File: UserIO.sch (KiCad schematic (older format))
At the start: 17 parts, among them SW1 PF0, SW2 PF1, SW3 PF2, SW4 PF3, SW5 RST, U1 ATXMEGA128A1U-AU

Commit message: Reannotate
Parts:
- renumbered C14 to C4, C15 to C5, C16 to C6, C17 to C7, DS1 to DS2, DS2 to DS3, DS3 to DS4, DS4 to DS5, R19 to R15, R10 to R16, R11 to R17, SW5 to SW1, SW1 to SW2, SW2 to SW3, SW3 to SW4, SW4 to SW5
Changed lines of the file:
@@
 $EndComp
 $Comp
-L TACT-TE-FSMSM SW1
+L TACT-TE-FSMSM SW2
 U 1 1 56EFE88A
 P 7250 4900
-F 0 "SW1" H 7400 5000 50  0000 C CNN
+F 0 "SW2" H 7400 5000 50  0000 C CNN
 F 1 "PF0" H 7100 5000 50  0000 C CNN
 F 2 "manuf:TE-FSMSM" H 7250 4700 60  0001 C CNN
@@
 P 4400 5950
 AR Path="/56EFE892" Ref="C?"  Part="1"
-AR Path="/56EFC605/56EFE892" Ref="C14"  Part="1"
-F 0 "C14" H 4450 6050 50  0000 L CNN
+AR Path="/56EFC605/56EFE892" Ref="C4"  Part="1"
+F 0 "C4" H 4450 6050 50  0000 L CNN
 F 1 "100n" H 4450 5850 50  0000 L CNN
 F 2 "IPC7351-Nominal:CAPC1005X55" H 4400 5950 50  0001 C CNN
@@
 PF0/~DFUEN
 $Comp
-L TACT-TE-FSMSM SW2
+L TACT-TE-FSMSM SW3
 U 1 1 56EFE8A1
 P 7250 5100
-F 0 "SW2" H 7400 5200 50  0000 C CNN
+F 0 "SW3" H 7400 5200 50  0000 C CNN
 F 1 "PF1" H 7100 5200 50  0000 C CNN
 F 2 "manuf:TE-FSMSM" H 7250 4900 60  0001 C CNN
@@
 $EndComp
 $Comp
-L TACT-TE-FSMSM SW3
+L TACT-TE-FSMSM SW4
 U 1 1 56EFE8A9
 P 7250 5300
-F 0 "SW3" H 7400 5400 50  0000 C CNN
+F 0 "SW4" H 7400 5400 50  0000 C CNN
 F 1 "PF2" H 7100 5400 50  0000 C CNN
 F 2 "manuf:TE-FSMSM" H 7250 5100 60  0001 C CNN
@@
 $EndComp
 $Comp
-L TACT-TE-FSMSM SW4
+L TACT-TE-FSMSM SW5
 U 1 1 56EFE8B1
 P 7250 5500
-F 0 "SW4" H 7400 5600 50  0000 C CNN
+F 0 "SW5" H 7400 5600 50  0000 C CNN
 F 1 "PF3" H 7100 5600 50  0000 C CNN
 F 2 "manuf:TE-FSMSM" H 7250 5300 60  0001 C CNN
@@
 P 4700 5950
 AR Path="/56EFE8B9" Ref="C?"  Part="1"
-AR Path="/56EFC605/56EFE8B9" Ref="C15"  Part="1"
-F 0 "C15" H 4750 6050 50  0000 L CNN
+AR Path="/56EFC605/56EFE8B9" Ref="C5"  Part="1"
+F 0 "C5" H 4750 6050 50  0000 L CNN
 F 1 "100n" H 4750 5850 50  0000 L CNN
 F 2 "IPC7351-Nominal:CAPC1005X55" H 4700 5950 50  0001 C CNN
@@
 P 5000 5950
 AR Path="/56EFE8C1" Ref="C?"  Part="1"
-AR Path="/56EFC605/56EFE8C1" Ref="C16"  Part="1"
-F 0 "C16" H 5050 6050 50  0000 L CNN
+AR Path="/56EFC605/56EFE8C1" Ref="C6"  Part="1"
+F 0 "C6" H 5050 6050 50  0000 L CNN
 F 1 "100n" H 5050 5850 50  0000 L CNN
 F 2 "IPC7351-Nominal:CAPC1005X55" H 5000 5950 50  0001 C CNN
@@
 P 5300 5950
 AR Path="/56EFE8C9" Ref="C?"  Part="1"
-AR Path="/56EFC605/56EFE8C9" Ref="C17"  Part="1"
-F 0 "C17" H 5350 6050 50  0000 L CNN
+AR Path="/56EFC605/56EFE8C9" Ref="C7"  Part="1"
+F 0 "C7" H 5350 6050 50  0000 L CNN
 F 1 "100n" H 5350 5850 50  0000 L CNN
 F 2 "IPC7351-Nominal:CAPC1005X55" H 5300 5950 50  0001 C CNN
@@
 PF3
 $Comp
-L TACT-TE-FSMSM SW5
+L TACT-TE-FSMSM SW1
 U 1 1 56EFE8EC
 P 7250 4500
-F 0 "SW5" H 7250 4720 50  0000 C CNN
+F 0 "SW1" H 7250 4720 50  0000 C CNN
 F 1 "RST" H 7250 4629 50  0000 C CNN
 F 2 "manuf:TE-FSMSM" H 7250 4300 60  0001 C CNN
@@
 $EndComp
 $Comp
-L LED-0603 DS1
+L LED-0603 DS2
 U 1 1 56EFE8F4
 P 5450 4000
-F 0 "DS1" H 5600 4046 50  0000 L CNN
+F 0 "DS2" H 5600 4046 50  0000 L CNN
 F 1 "PF4" H 5600 3955 50  0000 L CNN
 F 2 "smd-semi:LED-0603" H 5450 3850 50  0001 C CNN
@@
 $EndComp
 $Comp
-L LED-0603 DS2
+L LED-0603 DS3
 U 1 1 56EFE902
 P 5850 4000
-F 0 "DS2" H 6000 4046 50  0000 L CNN
+F 0 "DS3" H 6000 4046 50  0000 L CNN
 F 1 "PF5" H 6000 3955 50  0000 L CNN
 F 2 "smd-semi:LED-0603" H 5850 3850 50  0001 C CNN
@@
 $EndComp
 $Comp
-L LED-0603 DS3
+L LED-0603 DS4
 U 1 1 56EFE910
 P 6250 4000
-F 0 "DS3" H 6400 4046 50  0000 L CNN
+F 0 "DS4" H 6400 4046 50  0000 L CNN
 F 1 "PF6" H 6400 3955 50  0000 L CNN
 F 2 "smd-semi:LED-0603" H 6250 3850 50  0001 C CNN
@@
 $EndComp
 $Comp
-L LED-0603 DS4
+L LED-0603 DS5
 U 1 1 56EFE91E
 P 6650 4000
-F 0 "DS4" H 6800 4046 50  0000 L CNN
+F 0 "DS5" H 6800 4046 50  0000 L CNN
 F 1 "PF7" H 6800 3955 50  0000 L CNN
 F 2 "smd-semi:LED-0603" H 6650 3850 50  0001 C CNN
@@
 P 5450 3700
 AR Path="/56EFE930" Ref="R?"  Part="1"
-AR Path="/56EFC605/56EFE930" Ref="R19"  Part="1"
-F 0 "R19" H 5387 3654 50  0000 R CNN
+AR Path="/56EFC605/56EFE930" Ref="R15"  Part="1"
+F 0 "R15" H 5387 3654 50  0000 R CNN
 F 1 "3k3" H 5387 3745 50  0000 R CNN
 F 2 "IPC7351-Nominal:RESCAXE80P160X320X70-8" H 5450 3700 50  0001 C CNN
@@
 P 5850 3700
 AR Path="/56EFE938" Ref="R?"  Part="2"
-AR Path="/56EFC605/56EFE938" Ref="R19"  Part="2"
-F 0 "R19" H 5787 3654 50  0000 R CNN
+AR Path="/56EFC605/56EFE938" Ref="R15"  Part="2"
+F 0 "R15" H 5787 3654 50  0000 R CNN
 F 1 "3k3" H 5787 3745 50  0000 R CNN
 F 2 "IPC7351-Nominal:RESCAXE80P160X320X70-8" H 5850 3700 50  0001 C CNN
@@
 P 6250 3700
 AR Path="/56EFE940" Ref="R?"  Part="3"
-AR Path="/56EFC605/56EFE940" Ref="R19"  Part="3"
-F 0 "R19" H 6187 3654 50  0000 R CNN
+AR Path="/56EFC605/56EFE940" Ref="R15"  Part="3"
+F 0 "R15" H 6187 3654 50  0000 R CNN
 F 1 "3k3" H 6187 3745 50  0000 R CNN
 F 2 "IPC7351-Nominal:RESCAXE80P160X320X70-8" H 6250 3700 50  0001 C CNN
@@
 P 6650 3700
 AR Path="/56EFE948" Ref="R?"  Part="4"
-AR Path="/56EFC605/56EFE948" Ref="R19"  Part="4"
-F 0 "R19" H 6587 3654 50  0000 R CNN
+AR Path="/56EFC605/56EFE948" Ref="R15"  Part="4"
+F 0 "R15" H 6587 3654 50  0000 R CNN
 F 1 "3k3" H 6587 3745 50  0000 R CNN
 F 2 "IPC7351-Nominal:RESCAXE80P160X320X70-8" H 6650 3700 50  0001 C CNN
@@
 P 5650 4900
 AR Path="/56EFE950" Ref="R?"  Part="1"
-AR Path="/56EFC605/56EFE950" Ref="R10"  Part="1"
-F 0 "R10" V 5700 4700 50  0000 C CNN
+AR Path="/56EFC605/56EFE950" Ref="R16"  Part="1"
+F 0 "R16" V 5700 4700 50  0000 C CNN
 F 1 "100k" V 5700 5100 50  0000 C CNN
 F 2 "IPC7351-Nominal:RESCAXE80P160X320X70-8" H 5650 4900 50  0001 C CNN
@@
 P 6900 4700
 AR Path="/56EFE958" Ref="R?"  Part="2"
-AR Path="/56EFC605/56EFE958" Ref="R10"  Part="2"
-F 0 "R10" H 6837 4654 50  0000 R CNN
+AR Path="/56EFC605/56EFE958" Ref="R16"  Part="2"
+F 0 "R16" H 6837 4654 50  0000 R CNN
 F 1 "100k" H 6837 4745 50  0000 R CNN
 F 2 "IPC7351-Nominal:RESCAXE80P160X320X70-8" H 6900 4700 50  0001 C CNN
@@
 P 6600 4700
 AR Path="/56EFE960" Ref="R?"  Part="3"
-AR Path="/56EFC605/56EFE960" Ref="R10"  Part="3"
-F 0 "R10" H 6663 4654 50  0000 L CNN
+AR Path="/56EFC605/56EFE960" Ref="R16"  Part="3"
+F 0 "R16" H 6663 4654 50  0000 L CNN
 F 1 "100k" H 6663 4745 50  0000 L CNN
 F 2 "IPC7351-Nominal:RESCAXE80P160X320X70-8" H 6600 4700 50  0001 C CNN
@@
 P 5650 5100
 AR Path="/56EFE968" Ref="R?"  Part="4"
-AR Path="/56EFC605/56EFE968" Ref="R10"  Part="4"
-F 0 "R10" V 5700 4900 50  0000 C CNN
+AR Path="/56EFC605/56EFE968" Ref="R16"  Part="4"
+F 0 "R16" V 5700 4900 50  0000 C CNN
 F 1 "100k" V 5700 5300 50  0000 C CNN
 F 2 "IPC7351-Nominal:RESCAXE80P160X320X70-8" H 5650 5100 50  0001 C CNN
@@
 P 5650 5300
 AR Path="/56EFE970" Ref="R?"  Part="1"
-AR Path="/56EFC605/56EFE970" Ref="R11"  Part="1"
-F 0 "R11" V 5700 5100 50  0000 C CNN
+AR Path="/56EFC605/56EFE970" Ref="R17"  Part="1"
+F 0 "R17" V 5700 5100 50  0000 C CNN
 F 1 "100k" V 5700 5500 50  0000 C CNN
 F 2 "IPC7351-Nominal:RESCAXE80P160X320X70-8" H 5650 5300 50  0001 C CNN
@@
 P 5650 5500
 AR Path="/56EFE978" Ref="R?"  Part="4"
-AR Path="/56EFC605/56EFE978" Ref="R11"  Part="4"
-F 0 "R11" V 5700 5300 50  0000 C CNN
+AR Path="/56EFC605/56EFE978" Ref="R17"  Part="4"
+F 0 "R17" V 5700 5300 50  0000 C CNN
 F 1 "100k" V 5700 5700 50  0000 C CNN
 F 2 "IPC7351-Nominal:RESCAXE80P160X320X70-8" H 5650 5500 50  0001 C CNN
@@
 P 6300 4700
 AR Path="/56EFE980" Ref="R?"  Part="2"
-AR Path="/56EFC605/56EFE980" Ref="R11"  Part="2"
-F 0 "R11" H 6237 4654 50  0000 R CNN
+AR Path="/56EFC605/56EFE980" Ref="R17"  Part="2"
+F 0 "R17" H 6237 4654 50  0000 R CNN
 F 1 "100k" H 6237 4745 50  0000 R CNN
 F 2 "IPC7351-Nominal:RESCAXE80P160X320X70-8" H 6300 4700 50  0001 C CNN
@@
 P 6000 4700
 AR Path="/56EFE988" Ref="R?"  Part="3"
-AR Path="/56EFC605/56EFE988" Ref="R11"  Part="3"
-F 0 "R11" H 6063 4654 50  0000 L CNN
+AR Path="/56EFC605/56EFE988" Ref="R17"  Part="3"
+F 0 "R17" H 6063 4654 50  0000 L CNN
 F 1 "100k" H 6063 4745 50  0000 L CNN
 F 2 "IPC7351-Nominal:RESCAXE80P160X320X70-8" H 6000 4700 50  0001 C CNN

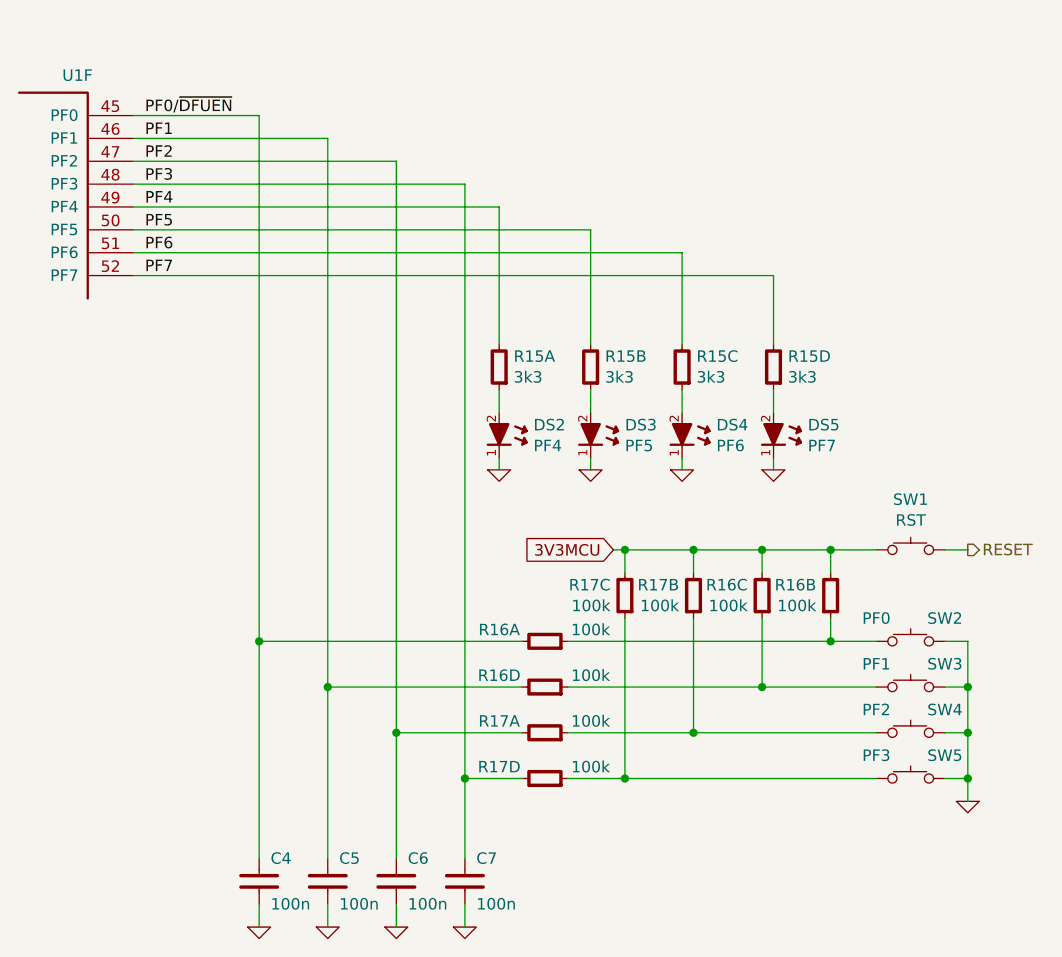
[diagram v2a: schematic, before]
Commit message: Schematic tidy-ups and add VBUS sense
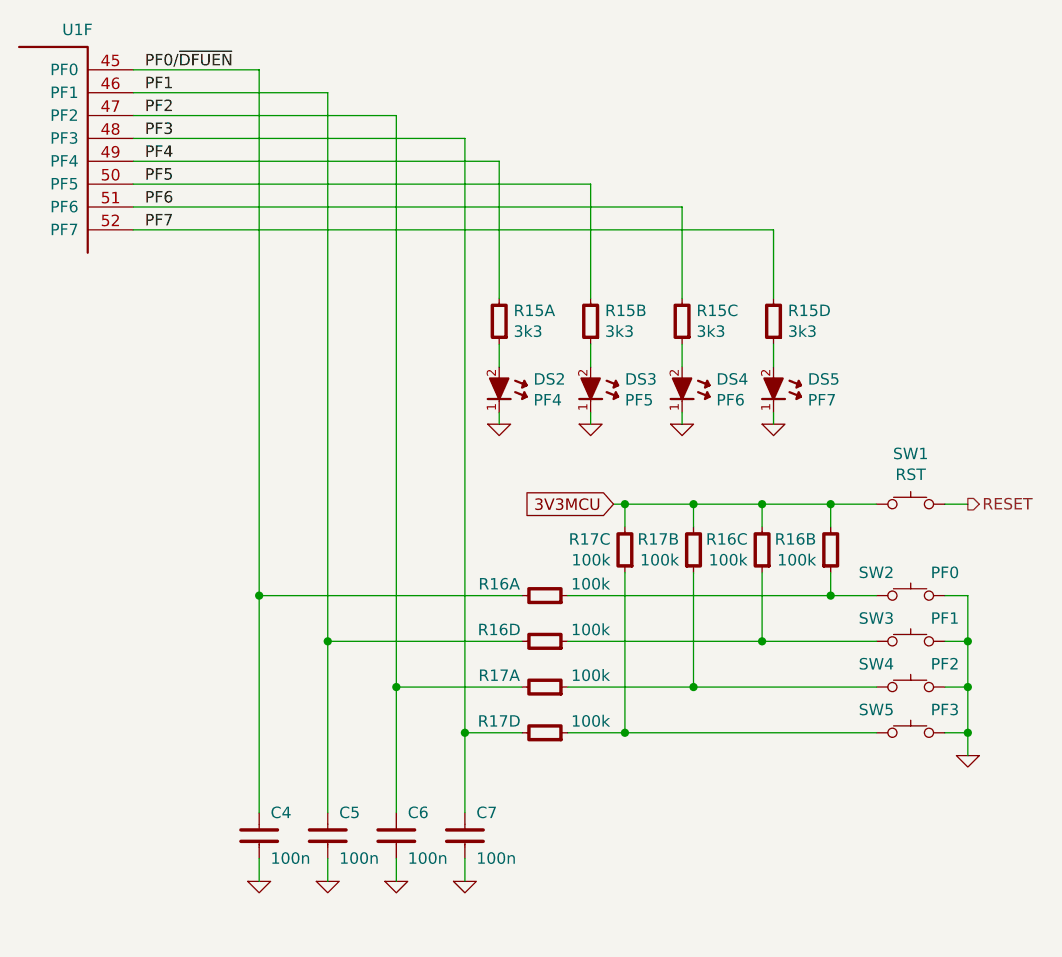
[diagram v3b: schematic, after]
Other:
- moved on the sheet: C4, C5, C6, C7, DS2, DS3, DS4, DS5, R15A, R15B, R15C, R15D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

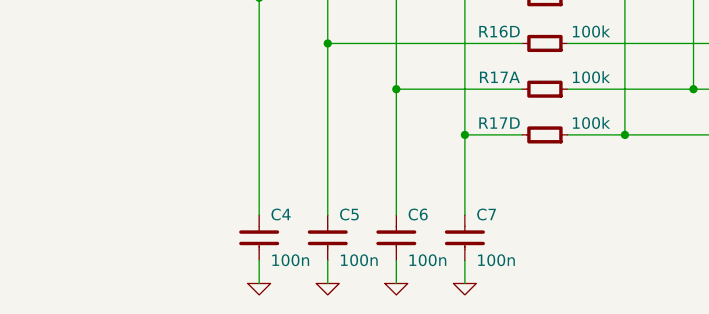
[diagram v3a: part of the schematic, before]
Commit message: Bugfix: debounce causes bootloader entry on power
Debounce capacitors were connected to ground, which held the IOs low at boot
for about 20ms. Capacitors are now connected to 3.3V instead.
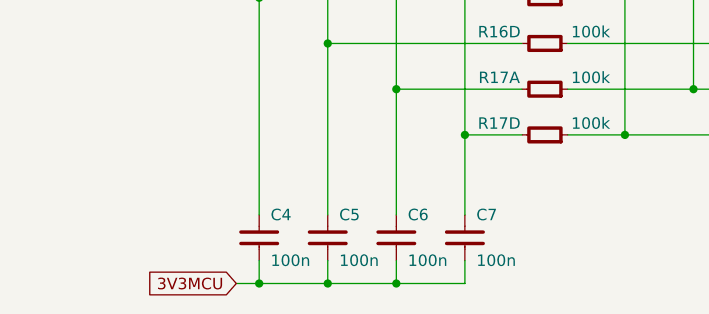
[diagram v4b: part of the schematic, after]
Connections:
- net 3V3MCU: now also C4.2, C5.2, C6.2, C7.2
- net GND: no longer C4.2, C5.2, C6.2, C7.2
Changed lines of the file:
@@
 LIBS:Vishay
 LIBS:Xilinx
+LIBS:semi-diode-Semtech
 LIBS:xmega-cache
 EELAYER 25 0
@@
 	1    0    0    -1
 $EndComp
-$Comp
-L GND #PWR?
-U 1 1 56EFE899
-P 4400 5950
-AR Path="/56EFE899" Ref="#PWR?"  Part="1"
-AR Path="/56EFC605/56EFE899" Ref="#PWR24"  Part="1"
-F 0 "#PWR24" H 4400 5950 30  0001 C CNN
-F 1 "GND" H 4400 5880 30  0001 C CNN
-F 2 "" H 4400 5950 60  0000 C CNN
-F 3 "" H 4400 5950 60  0000 C CNN
-	1    4400 5950
-	1    0    0    -1
-$EndComp
 Text Label 3900 2400 0    50   ~ 0
 PF0/~DFUEN
@@
 $Comp
 L GND #PWR?
-U 1 1 56EFE8D0
-P 4700 5950
-AR Path="/56EFE8D0" Ref="#PWR?"  Part="1"
-AR Path="/56EFC605/56EFE8D0" Ref="#PWR25"  Part="1"
-F 0 "#PWR25" H 4700 5950 30  0001 C CNN
-F 1 "GND" H 4700 5880 30  0001 C CNN
-F 2 "" H 4700 5950 60  0000 C CNN
-F 3 "" H 4700 5950 60  0000 C CNN
-	1    4700 5950
-	1    0    0    -1
-$EndComp
-$Comp
-L GND #PWR?
-U 1 1 56EFE8D6
-P 5000 5950
-AR Path="/56EFE8D6" Ref="#PWR?"  Part="1"
-AR Path="/56EFC605/56EFE8D6" Ref="#PWR26"  Part="1"
-F 0 "#PWR26" H 5000 5950 30  0001 C CNN
-F 1 "GND" H 5000 5880 30  0001 C CNN
-F 2 "" H 5000 5950 60  0000 C CNN
-F 3 "" H 5000 5950 60  0000 C CNN
-	1    5000 5950
-	1    0    0    -1
-$EndComp
-$Comp
-L GND #PWR?
-U 1 1 56EFE8DC
-P 5300 5950
-AR Path="/56EFE8DC" Ref="#PWR?"  Part="1"
-AR Path="/56EFC605/56EFE8DC" Ref="#PWR27"  Part="1"
-F 0 "#PWR27" H 5300 5950 30  0001 C CNN
-F 1 "GND" H 5300 5880 30  0001 C CNN
-F 2 "" H 5300 5950 60  0000 C CNN
-F 3 "" H 5300 5950 60  0000 C CNN
-	1    5300 5950
-	1    0    0    -1
-$EndComp
-$Comp
-L GND #PWR?
 U 1 1 56EFE8E2
 P 7500 5400
@@
 Text HLabel 7500 4300 2    50   Output ~ 0
 RESET
+Text GLabel 4300 5950 0    50   Input ~ 0
+3V3MCU
+Wire Wire Line
+	4300 5950 5300 5950
+Connection ~ 4400 5950
+Connection ~ 4700 5950
+Connection ~ 5000 5950
 $EndSCHEMATC

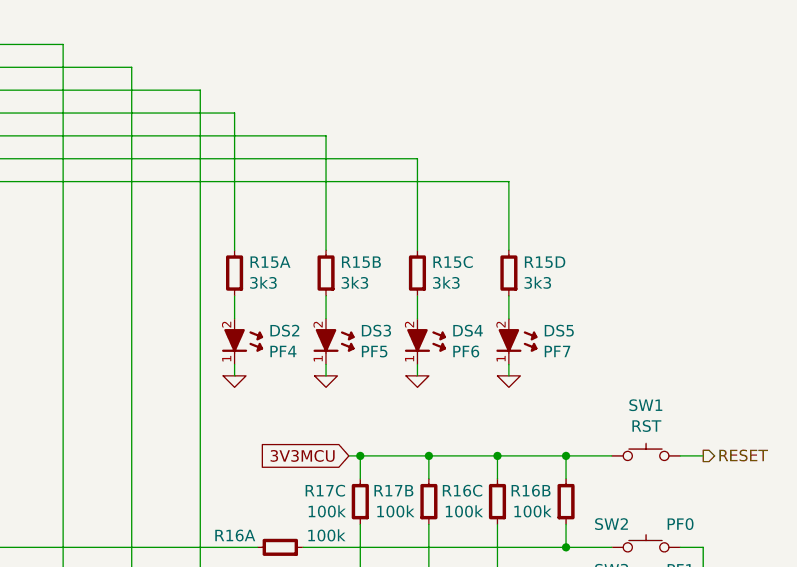
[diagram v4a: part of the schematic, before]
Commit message: Decrease LED current
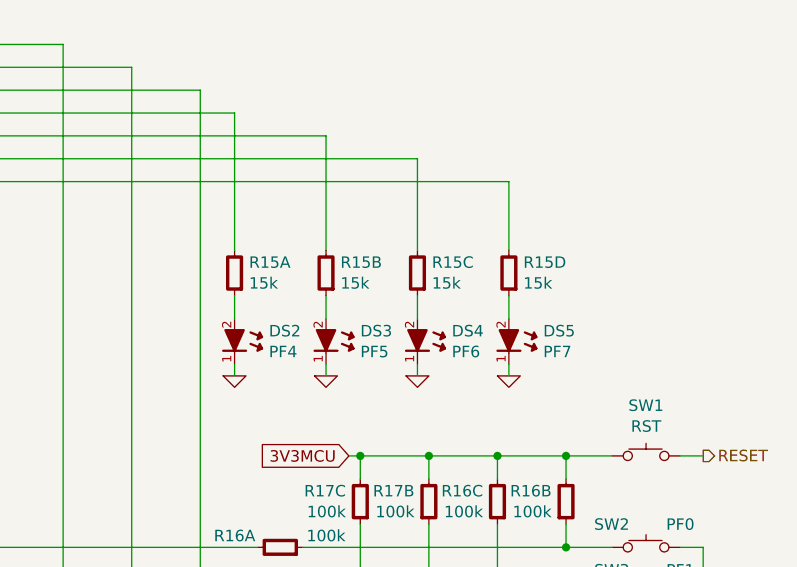
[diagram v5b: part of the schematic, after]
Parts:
- R15: value 3k3 -> 15k; BOM DIST DIGIKEY YC164J-3.3KCT-ND -> DIST DIGIKEY YC164J-15KCT-ND
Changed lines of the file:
@@
 AR Path="/56EFC605/56EFE930" Ref="R15"  Part="1"
 F 0 "R15" H 5387 3454 50  0000 R CNN
-F 1 "3k3" H 5387 3545 50  0000 R CNN
+F 1 "15k" H 5387 3545 50  0000 R CNN
 F 2 "IPC7351-Nominal:RESCAXE80P160X320X70-8" H 5450 3500 50  0001 C CNN
 F 3 "" H 5450 3550 60  0000 C CNN
-F 4 "DIST DIGIKEY YC164J-3.3KCT-ND" H 5450 3500 60  0001 C CNN "BOM"
+F 4 "DIST DIGIKEY YC164J-15KCT-ND" H 5450 3500 60  0001 C CNN "BOM"
 	1    5450 3500
 	-1   0    0    1
@@
 AR Path="/56EFC605/56EFE938" Ref="R15"  Part="2"
 F 0 "R15" H 5787 3454 50  0000 R CNN
-F 1 "3k3" H 5787 3545 50  0000 R CNN
+F 1 "15k" H 5787 3545 50  0000 R CNN
 F 2 "IPC7351-Nominal:RESCAXE80P160X320X70-8" H 5850 3500 50  0001 C CNN
 F 3 "" H 5850 3550 60  0000 C CNN
-F 4 "DIST DIGIKEY YC164J-3.3KCT-ND" H 5850 3500 60  0001 C CNN "BOM"
+F 4 "DIST DIGIKEY YC164J-15KCT-ND" H 5850 3500 60  0001 C CNN "BOM"
 	2    5850 3500
 	-1   0    0    1
@@
 AR Path="/56EFC605/56EFE940" Ref="R15"  Part="3"
 F 0 "R15" H 6187 3454 50  0000 R CNN
-F 1 "3k3" H 6187 3545 50  0000 R CNN
+F 1 "15k" H 6187 3545 50  0000 R CNN
 F 2 "IPC7351-Nominal:RESCAXE80P160X320X70-8" H 6250 3500 50  0001 C CNN
 F 3 "" H 6250 3550 60  0000 C CNN
-F 4 "DIST DIGIKEY YC164J-3.3KCT-ND" H 6250 3500 60  0001 C CNN "BOM"
+F 4 "DIST DIGIKEY YC164J-15KCT-ND" H 6250 3500 60  0001 C CNN "BOM"
 	3    6250 3500
 	-1   0    0    1
@@
 AR Path="/56EFC605/56EFE948" Ref="R15"  Part="4"
 F 0 "R15" H 6587 3454 50  0000 R CNN
-F 1 "3k3" H 6587 3545 50  0000 R CNN
+F 1 "15k" H 6587 3545 50  0000 R CNN
 F 2 "IPC7351-Nominal:RESCAXE80P160X320X70-8" H 6650 3500 50  0001 C CNN
 F 3 "" H 6650 3550 60  0000 C CNN
-F 4 "DIST DIGIKEY YC164J-3.3KCT-ND" H 6650 3500 60  0001 C CNN "BOM"
+F 4 "DIST DIGIKEY YC164J-15KCT-ND" H 6650 3500 60  0001 C CNN "BOM"
 	4    6650 3500
 	-1   0    0    1
